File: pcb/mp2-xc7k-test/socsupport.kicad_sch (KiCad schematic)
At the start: 71 parts, among them J5 CORTEX_DEBUG_ETM, U12 ECS-1612MV-250-CN, U5 STM32MP257FAI3

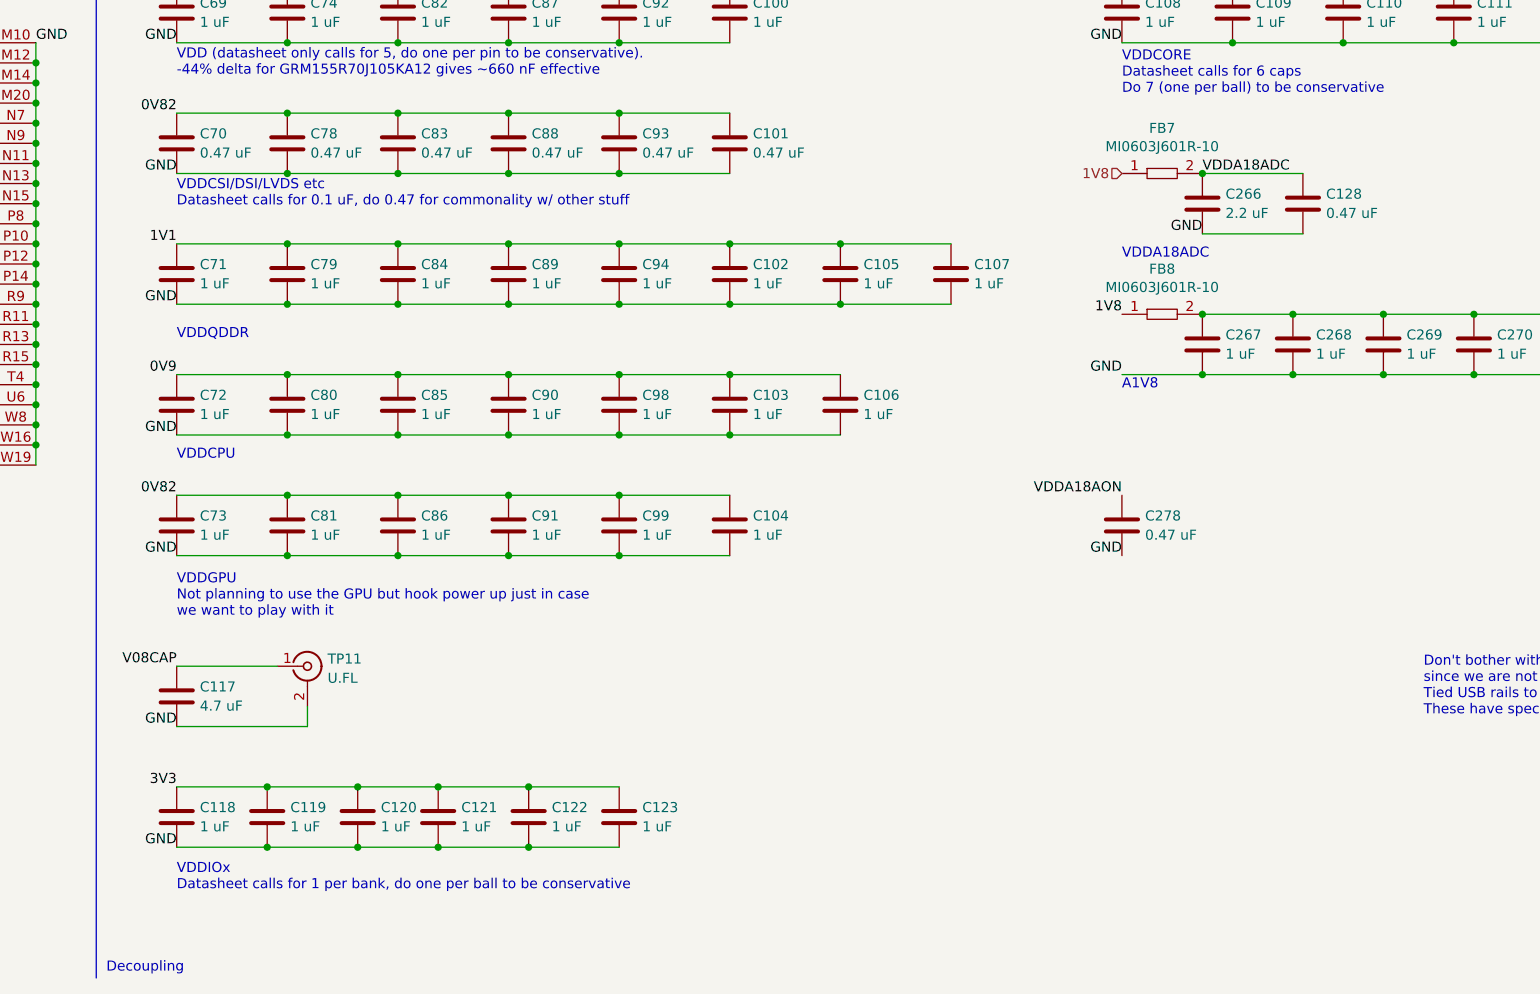
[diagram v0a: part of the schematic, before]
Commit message: Continued layout, 454 unrouted
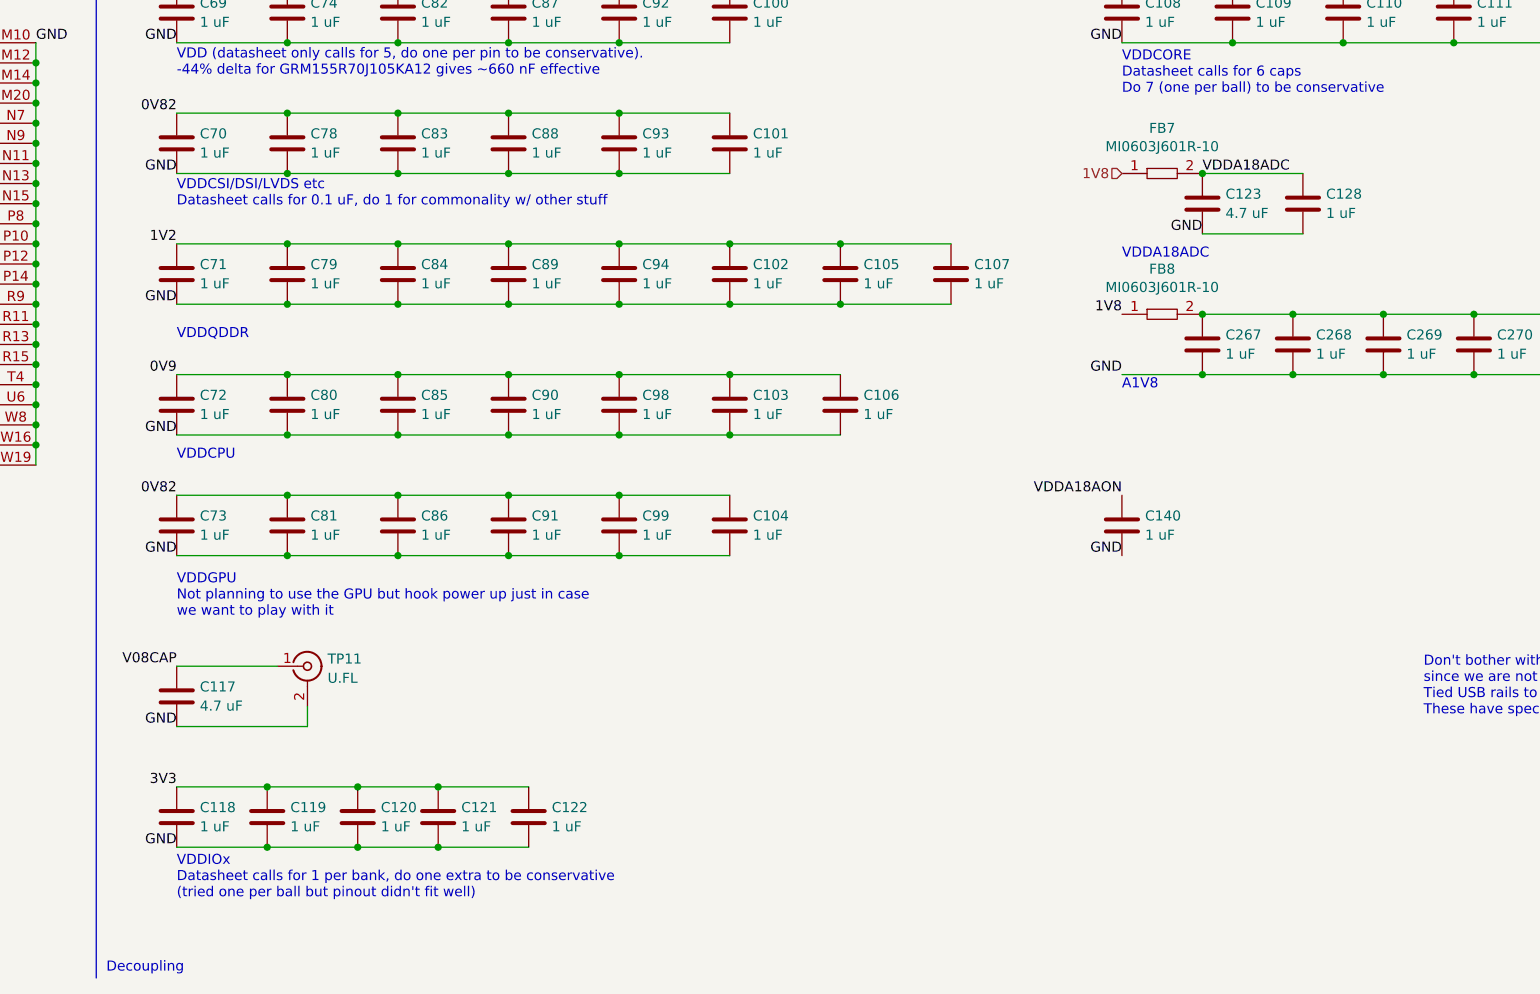
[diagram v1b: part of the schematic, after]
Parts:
- removed C266: 2.2 uF, symbol device:C
- removed C278: 0.47 uF, symbol device:C
- added C140: 1 uF, azonenberg_pcb:EIA_0201_CAP_NOSILK, symbol device:C
- C100, C102, C103, C104, C105, C106, C107, C108, C109, C110, C111, C112, C113, C114, C118, C119, C120, C121, C122, C267, C268, C269, C270, C271, C272, C273, C274, C69, C71, C72, C73, C74, C79, C80, C81, C82, C84, C85, C86, C87, C89, C90, C91, C92, C94, C98, C99: footprint (none) -> azonenberg_pcb:EIA_0201_CAP_NOSILK
- C101, C128, C70, C78, C83, C88, C93: value 0.47 uF -> 1 uF; footprint (none) -> azonenberg_pcb:EIA_0201_CAP_NOSILK
- C117: footprint (none) -> azonenberg_pcb:EIA_0603_CAP_NOSILK
- C123: value 1 uF -> 4.7 uF; footprint (none) -> azonenberg_pcb:EIA_0603_CAP_NOSILK
- R42: footprint (none) -> azonenberg_pcb:EIA_0402_RES_NOSILK
- U5: footprint (none) -> azonenberg_pcb:BGA_436_18x18_DEPOP_0.8MM
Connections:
- net 1V1 is gone; now on net 1V2: C102.1, C105.1, C107.1, C71.1, C79.1, C84.1, C89.1, C94.1
- net 3V3: no longer C123.1
- net GND: now also C140.2
- net VDDA18ADC: now also C123.1
- net VDDA18AON: now also C140.1
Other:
- note added: "VDDCSI/DSI/LVDS etc Datasheet calls for 0.1 uF, do 1 for commonality w/ other stuff"
- note added: "VDDIOx Datasheet calls for 1 per bank, do one extra to be conservative (tried one per ball but pinout didn't fit well)"
- note removed: "VDDCSI/DSI/LVDS etc Datasheet calls for 0.1 uF, do 0.47 for commonality w/ other stuff"
- note removed: "VDDIOx Datasheet calls for 1 per bank, do one per ball to be conservative"

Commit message: Continued PCB routing, 344 nets left
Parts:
- added TP13: U.FL, azonenberg_pcb:CONN_U.FL_TE_1909763-1, symbol conn:CONN_COAXIAL
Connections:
- net A1V8: now also TP13.1 (In)
- net GND: now also TP13.2 (Ext)
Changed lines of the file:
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@@
 	)
 	(junction
+		(at 351.79 200.66)
+		(diameter 0)
+		(color 0 0 0 0)
+	)
+	(junction
 		(at 34.29 21.59)
 		(diameter 0)
@@
 	)
 	(junction
+		(at 351.79 208.28)
+		(diameter 0)
+		(color 0 0 0 0)
+	)
+	(junction
 		(at 303.53 158.75)
 		(diameter 0)
@@
 	(wire
 		(pts
+			(xy 351.79 208.28) (xy 365.76 208.28)
+		)
+		(stroke
+			(width 0)
+			(type default)
+		)
+	)
+	(wire
+		(pts
 			(xy 36.83 218.44) (xy 36.83 220.98)
 		)
@@
 	(wire
 		(pts
+			(xy 365.76 208.28) (xy 365.76 205.74)
+		)
+		(stroke
+			(width 0)
+			(type default)
+		)
+	)
+	(wire
+		(pts
 			(xy 184.15 191.77) (xy 198.12 191.77)
 		)
@@
 	(wire
 		(pts
+			(xy 351.79 200.66) (xy 361.95 200.66)
+		)
+		(stroke
+			(width 0)
+			(type default)
+		)
+	)
+	(wire
+		(pts
 			(xy 271.78 182.88) (xy 284.48 182.88)
 		)
@@
 					(unit 1)
 				)
+			)
+		)
+	)
+	(symbol
+		(lib_id "conn:CONN_COAXIAL")
+		(at 365.76 200.66 0)
+		(unit 1)
+		(exclude_from_sim no)
+		(in_bom yes)
+		(on_board yes)
+		(dnp no)
+		(fields_autoplaced yes)
+		(property "Reference" "TP13"
+			(at 368.3 199.741 0)
+			(effects
+				(font
+					(size 1.27 1.27)
+				)
+				(justify left)
+			)
+		)
+		(property "Value" "U.FL"
+			(at 368.3 202.1653 0)
+			(effects
+				(font
+					(size 1.27 1.27)
+				)
+				(justify left)
+			)
+		)
+		(property "Footprint" "azonenberg_pcb:CONN_U.FL_TE_1909763-1"
+			(at 365.76 200.66 0)
+			(effects
+				(font
+					(size 1.27 1.27)
+				)
+				(hide yes)
+			)
+		)
+		(property "Datasheet" ""
+			(at 365.76 200.66 0)
+			(effects
+				(font
+					(size 1.27 1.27)
+				)
+				(hide yes)
+			)
+		)
+		(property "Description" "coaxial connector (BNC, SMA, SMB, SMC, Cinch/RCA, ...)"
+			(at 365.76 200.66 0)
+			(effects
+				(font
+					(size 1.27 1.27)
+				)
+				(hide yes)
+			)
+		)
+		(pin "1"
+		)
+		(pin "2"
+		)
+		(instances
+			(project "mp2-xc7k-test"
+				(path "/b52ad5ff-5dbb-4f64-8839-2dc6cd4521cb/9cff8885-a75f-4d5c-8256-e2d0dc09d791"
+					(reference "TP13")
+					(unit 1)
+				)

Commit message: Test board ready for design review
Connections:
- net GND: now also U5.U17 (VDDA18USB)
- no-connect marks 4 -> 3
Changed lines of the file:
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@@
 	(paper "A3")
 	(title_block
-		(date "2025-12-19")
+		(date "2025-12-25")
 		(rev "0.1")
 	)
@@
 	)
 	(no_connect
-		(at 36.83 203.2)
-	)
-	(no_connect
 		(at 36.83 54.61)
 	)
@@
 	)
 	(label "GND"
+		(at 36.83 203.2 180)
+		(effects
+			(font
+				(size 1.27 1.27)
+			)
+			(justify right bottom)
+		)
+	)
+	(label "GND"
 		(at 142.24 215.9 180)
 		(effects
@@
 			)
 		)
-		(pin "AE5"
+		(pin "Y8"
 		)
 		(pin "U16"
@@
 		(pin "AA7"
 		)
-		(pin "AG10"
+		(pin "T8"
 		)
 		(pin "L7"
@@
 		(pin "W9"
 		)
-		(pin "AF9"
+		(pin "AA6"
 		)
 		(pin "T6"
@@
 			)
 		)
-		(pin "AE5"
+		(pin "Y8"
 		)
 		(pin "U16"
@@
 		(pin "AA7"
 		)
-		(pin "AG10"
+		(pin "T8"
 		)
 		(pin "L7"
@@
 		(pin "W9"
 		)
-		(pin "AF9"
+		(pin "AA6"
 		)
 		(pin "T6"
@@
 			)
 		)
-		(pin "AE5"
+		(pin "AA6"
 		)
 		(pin "U16"
@@
 		(pin "AA7"
 		)
-		(pin "AG10"
+		(pin "Y8"
 		)
 		(pin "L7"
@@
 		(pin "W9"
 		)
-		(pin "AF9"
+		(pin "T8"
 		)
 		(pin "T6"
@@
 			)
 		)
-		(pin "AE5"
+		(pin "Y8"
 		)
 		(pin "U16"
@@
 		(pin "AA7"
 		)
-		(pin "AG10"
+		(pin "AA6"
 		)
 		(pin "L7"
@@
 		(pin "W9"
 		)
-		(pin "AF9"
+		(pin "T8"
 		)
 		(pin "T6"

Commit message: Final MP2 XC7K test board ready for fab
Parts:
- added R28, R29: 0, azonenberg_pcb:EIA_0402_RES_NOSILK, symbol device:R
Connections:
- net GND: now also R28.2, R29.2; no longer U5.T16 (VDD33UCPD), U5.Y16 (VDD33USB)
- new net: R28.1, U5.T16 (VDD33UCPD)
- new net: R29.1, U5.Y16 (VDD33USB)
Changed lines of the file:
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@@
 	(wire
 		(pts
+			(xy 77.47 223.52) (xy 82.55 223.52)
+		)
+		(stroke
+			(width 0)
+			(type default)
+		)
+	)
+	(wire
+		(pts
 			(xy 71.12 21.59) (xy 68.58 21.59)
 		)
@@
 	(wire
 		(pts
+			(xy 77.47 243.84) (xy 82.55 243.84)
+		)
+		(stroke
+			(width 0)
+			(type default)
+		)
+	)
+	(wire
+		(pts
 			(xy 283.21 200.66) (xy 294.64 200.66)
 		)
@@
 	)
 	(label "GND"
+		(at 90.17 243.84 0)
+		(effects
+			(font
+				(size 1.27 1.27)
+			)
+			(justify left bottom)
+		)
+	)
+	(label "GND"
 		(at 142.24 231.14 180)
 		(effects
@@
 		)
 	)
+	(label "GND"
+		(at 90.17 223.52 0)
+		(effects
+			(font
+				(size 1.27 1.27)
+			)
+			(justify left bottom)
+		)
+	)
 	(label "SOC_JTAG_TDI"
 		(at 36.83 102.87 180)
@@
 		)
 	)
-	(label "GND"
-		(at 77.47 223.52 0)
-		(effects
-			(font
-				(size 1.27 1.27)
-			)
-			(justify left bottom)
-		)
-	)
 	(label "3V3"
 		(at 72.39 105.41 0)
@@
 	)
 	(label "GND"
-		(at 77.47 243.84 0)
-		(effects
-			(font
-				(size 1.27 1.27)
-			)
-			(justify left bottom)
-		)
-	)
-	(label "GND"
 		(at 271.78 190.5 180)
 		(effects
@@
 	)
 	(symbol
+		(lib_id "device:R")
+		(at 86.36 223.52 90)
+		(unit 1)
+		(exclude_from_sim no)
+		(in_bom yes)
+		(on_board yes)
+		(dnp no)
+		(property "Reference" "R28"
+			(at 86.36 220.98 90)
+			(effects
+				(font
+					(size 1.27 1.27)
+				)
+			)
+		)
+		(property "Value" "0"
+			(at 86.36 223.52 90)
+			(effects
+				(font
+					(size 1.27 1.27)
+				)
+			)
+		)
+		(property "Footprint" "azonenberg_pcb:EIA_0402_RES_NOSILK"
+			(at 86.36 225.298 90)
+			(effects
+				(font
+					(size 1.27 1.27)
+				)
+				(hide yes)
+			)
+		)
+		(property "Datasheet" ""
+			(at 86.36 223.52 0)
+			(effects
+				(font
+					(size 1.27 1.27)
+				)
+				(hide yes)
+			)
+		)
+		(property "Description" "Resistor"
+			(at 86.36 223.52 0)
+			(effects
+				(font
+					(size 1.27 1.27)
+				)
+				(hide yes)
+			)
+		)
+		(pin "1"
+		)
+		(pin "2"
+		)
+		(instances
+			(project ""
+				(path "/b52ad5ff-5dbb-4f64-8839-2dc6cd4521cb/9cff8885-a75f-4d5c-8256-e2d0dc09d791"
+					(reference "R28")
+					(unit 1)
+				)
+			)
+		)
+	)
+	(symbol
 		(lib_id "device:C")
 		(at 142.24 179.07 0)
@@
 					(unit 1)
 				)
+			)
+		)
+	)
+	(symbol
+		(lib_id "device:R")
+		(at 86.36 243.84 90)
+		(unit 1)
+		(exclude_from_sim no)
+		(in_bom yes)
+		(on_board yes)
+		(dnp no)
+		(property "Reference" "R29"
+			(at 86.36 246.38 90)
+			(effects
+				(font
+					(size 1.27 1.27)
+				)
+			)
+		)
+		(property "Value" "0"
+			(at 86.36 243.84 90)
+			(effects
+				(font
+					(size 1.27 1.27)
+				)
+			)
+		)
+		(property "Footprint" "azonenberg_pcb:EIA_0402_RES_NOSILK"
+			(at 86.36 245.618 90)
+			(effects
+				(font
+					(size 1.27 1.27)
+				)
+				(hide yes)
+			)
+		)
+		(property "Datasheet" ""
+			(at 86.36 243.84 0)
+			(effects
+				(font
+					(size 1.27 1.27)
+				)
+				(hide yes)
+			)
+		)
+		(property "Description" "Resistor"
+			(at 86.36 243.84 0)
+			(effects
+				(font
+					(size 1.27 1.27)
+				)
+				(hide yes)
+			)
+		)
+		(pin "1"
+		)
+		(pin "2"
+		)
+		(instances
+			(project "mp2-xc7k-test"
+				(path "/b52ad5ff-5dbb-4f64-8839-2dc6cd4521cb/9cff8885-a75f-4d5c-8256-e2d0dc09d791"
+					(reference "R29")
+					(unit 1)
+				)
